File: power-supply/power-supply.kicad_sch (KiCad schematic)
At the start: 20 parts, among them J1 Barrel_Jack_Switch, J2 Output, U1 LM7812_TO220, U2 LM7912_TO220

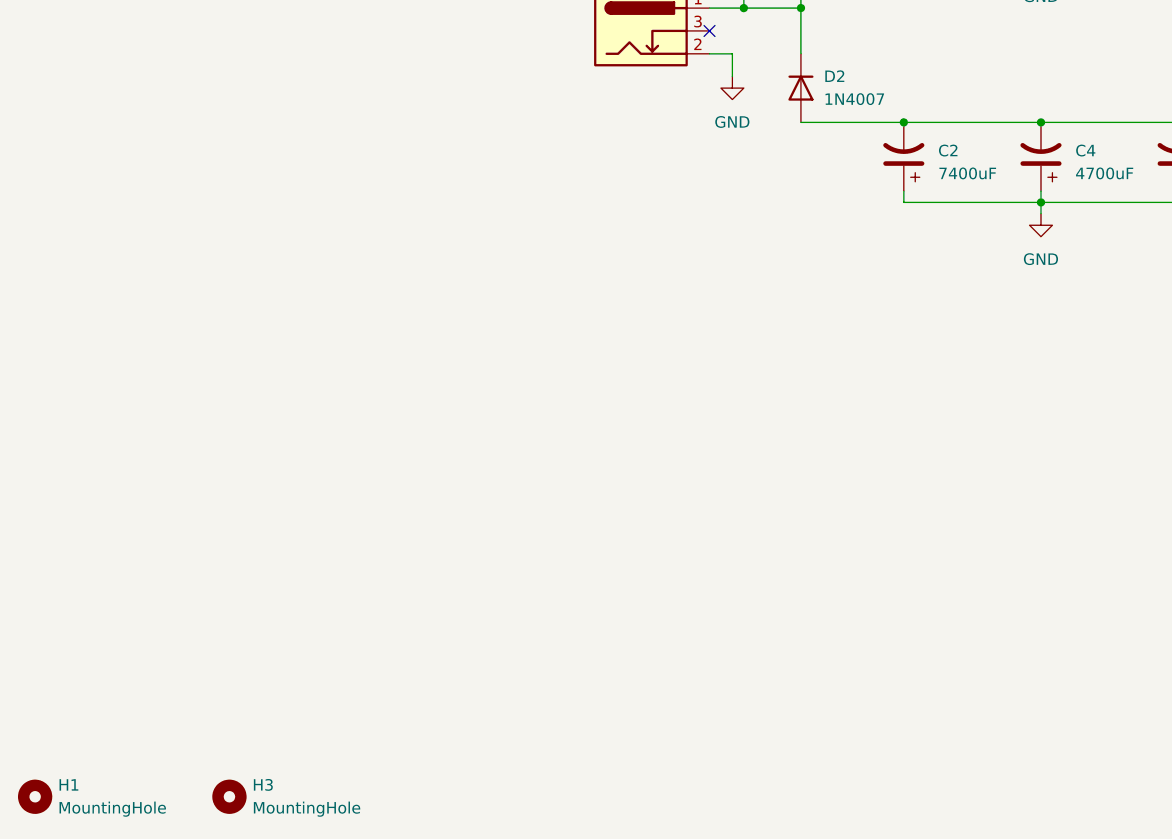
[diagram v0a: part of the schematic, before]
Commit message: Made mounting holes M3 sized. Generated BOM
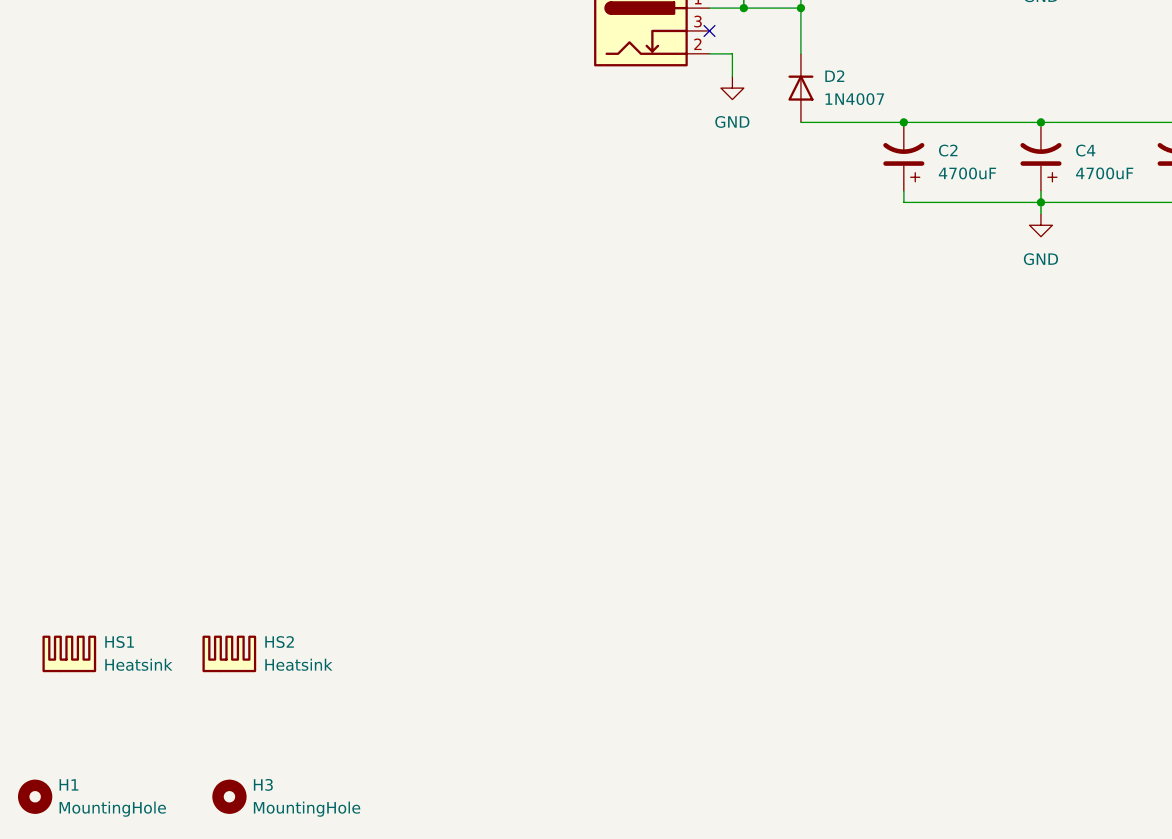
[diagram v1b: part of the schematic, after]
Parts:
- added HS1, HS2: Heatsink, symbol Mechanical:Heatsink
- C1, C3, C4, C5, C6: Manufacturer (none) -> JB Capacitors; Manufacturer Part No. (none) -> JRB1E472M07501600250000B; Supplier (none) -> Tayda; Supplier Part No. (none) -> A-1077
- C10, C7, C8, C9: Manufacturer (none) -> AVX; Manufacturer Part No. (none) -> 1uF 35V Radial Capacitor Tantalum; Supplier (none) -> Tayda; Supplier Part No. (none) -> A-265
- C2: value 7400uF -> 4700uF; Manufacturer (none) -> JB Capacitors; Manufacturer Part No. (none) -> JRB1E472M07501600250000B; Supplier (none) -> Tayda; Supplier Part No. (none) -> A-1077
- D1, D2: Manufacturer (none) -> EIC; Manufacturer Part No. (none) -> 1N4007; Supplier (none) -> Tayda; Supplier Part No. (none) -> A-155
- H1, H2, H3, H4: footprint MountingHole:MountingHole_2.2mm_M2 -> MountingHole:MountingHole_3.2mm_M3; now left out of the parts list
- J1: Manufacturer (none) -> WEALTH METAL; Manufacturer Part No. (none) -> DC Power Jack 2.1mm; Supplier (none) -> Tayda; Supplier Part No. (none) -> A-4118
- J2: Manufacturer (none) -> DEGSON; Manufacturer Part No. (none) -> DG126-03P; Supplier (none) -> Tayda; Supplier Part No. (none) -> A-663
- U1: Manufacturer (none) -> STMicroelectronics; Manufacturer Part No. (none) -> L7812CV; Supplier (none) -> Tayda; Supplier Part No. (none) -> A-207
- U2: Manufacturer (none) -> STMicroelectronics; Manufacturer Part No. (none) -> L7912CV; Supplier (none) -> Tayda; Supplier Part No. (none) -> A-505

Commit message: Updated for rev2
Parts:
- added D3: 1N4007, Diode_THT:D_DO-41_SOD81_P10.16mm_Horizontal, symbol Diode:1N4007
- C7: value 1uF -> 0.33uF
- C8: value 1uF -> 2.2uF
- C9: value 1uF -> 0.1uF
- J2: footprint TerminalBlock:TerminalBlock_Altech_AK300-3_P5.00mm -> DEGSON_Screw_Terminals:DG126
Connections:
- net at C1.1, C3.1, C5.1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: now also D3.1 (K)
- net at C9.1, J2.3 (Pin_3), U1.3 (VO): now also D3.2 (A)
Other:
- moved on the sheet: J2

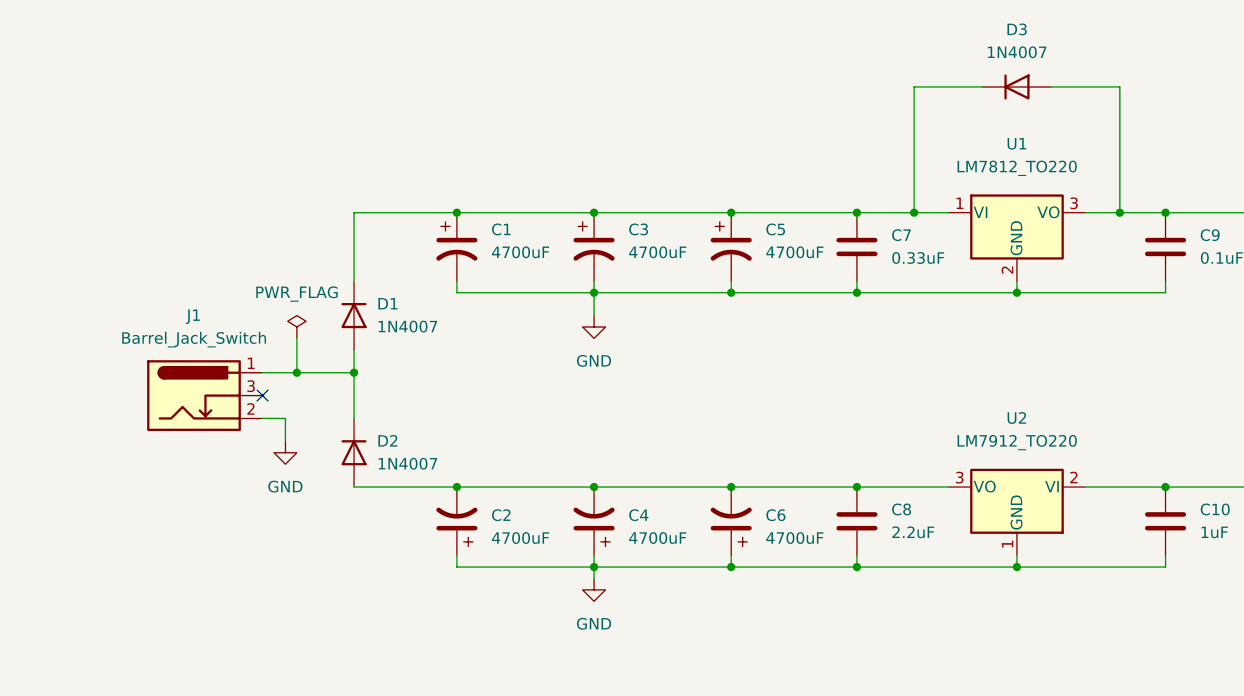
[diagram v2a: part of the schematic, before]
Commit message: Flipped input/output of 7912
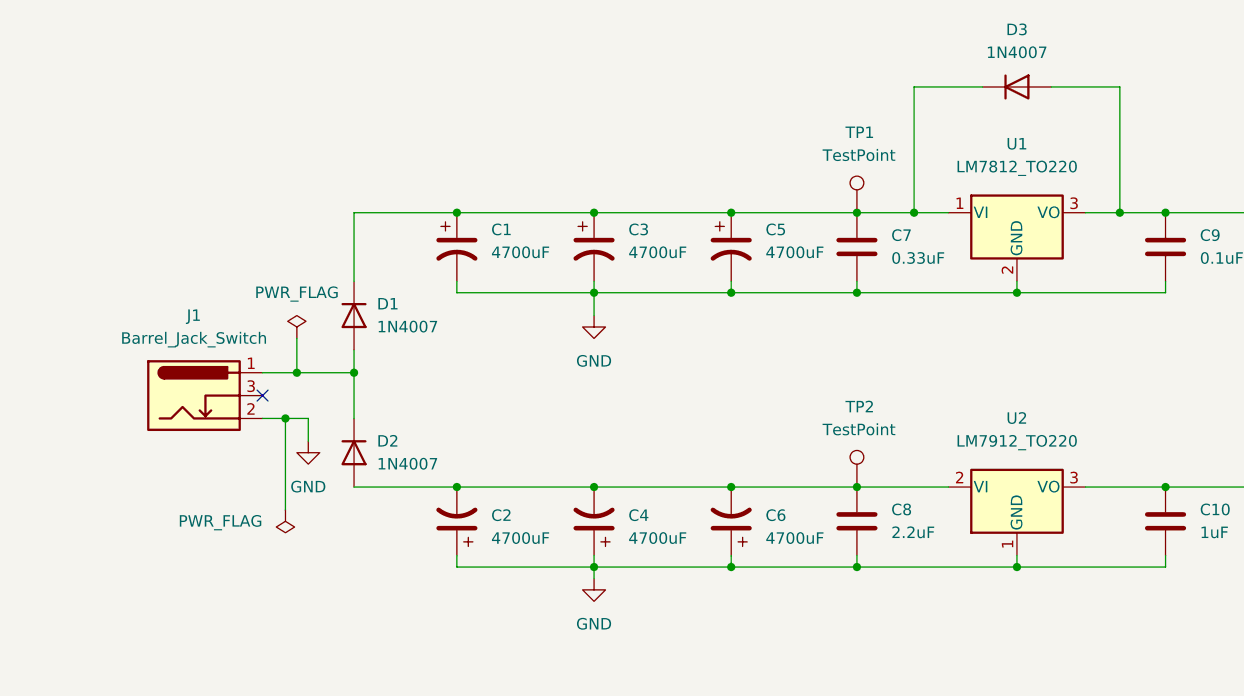
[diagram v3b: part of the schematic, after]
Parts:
- added TP1, TP2: TestPoint, TestPoint:TestPoint_Pad_D1.5mm, symbol Connector:TestPoint
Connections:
- net at C1.1, C3.1, C5.1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: now also TP1.1
- net at C2.2, C4.2, C6.2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: now also U2.2 (VI), TP2.1; no longer U2.3 (VO)
- net at C10.1, J2.1 (Pin_1): now also U2.3 (VO); no longer U2.2 (VI)
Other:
- moved on the sheet: U2
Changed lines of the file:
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@@
   (junction (at 196.85 76.2) (diameter 0) (color 0 0 0 0)
+  )
+  (junction (at 99.06 99.06) (diameter 0) (color 0 0 0 0)
   )
   (junction (at 148.59 115.57) (diameter 0) (color 0 0 0 0)
@@
     (stroke (width 0) (type default) (color 0 0 0 0))
   )
+  (wire (pts (xy 99.06 99.06) (xy 99.06 109.22))
+    (stroke (width 0) (type default) (color 0 0 0 0))
+  )
   (wire (pts (xy 133.35 115.57) (xy 148.59 115.57))
     (stroke (width 0) (type default) (color 0 0 0 0))
@@
     (stroke (width 0) (type default) (color 0 0 0 0))
   )
-  (wire (pts (xy 99.06 99.06) (xy 99.06 101.6))
+  (wire (pts (xy 101.6 99.06) (xy 101.6 101.6))
+    (stroke (width 0) (type default) (color 0 0 0 0))
+  )
+  (wire (pts (xy 99.06 99.06) (xy 101.6 99.06))
     (stroke (width 0) (type default) (color 0 0 0 0))
   )
@@
   (symbol (lib_id "power:PWR_FLAG") (at 100.33 90.17 0) (unit 1)
     (in_bom yes) (on_board yes) (fields_autoplaced)
-    (property "Reference" "#FLG01" (id 0) (at 100.33 88.265 0)
+    (property "Reference" "#FLG02" (id 0) (at 100.33 88.265 0)
       (effects (font (size 1.27 1.27)) hide)
     )
@@
     (pin "2")
   )
+  (symbol (lib_id "Connector:TestPoint") (at 162.56 76.2 0) (unit 1)
+    (in_bom yes) (on_board yes)
+    (property "Reference" "TP1" (id 0) (at 161.29 67.31 0)
+      (effects (font (size 1.27 1.27)) (justify left))
+    )
+    (property "Value" "TestPoint" (id 1) (at 158.75 69.85 0)
+      (effects (font (size 1.27 1.27)) (justify left))
+    )
+    (property "Footprint" "TestPoint:TestPoint_Pad_D1.5mm" (id 2) (at 167.64 76.2 0)
+      (effects (font (size 1.27 1.27)) hide)
+    )
+    (property "Datasheet" "~" (id 3) (at 167.64 76.2 0)
+      (effects (font (size 1.27 1.27)) hide)
+    )
+    (pin "1")
+  )
   (symbol (lib_id "Mechanical:MountingHole") (at 21.59 181.61 0) (unit 1)
     (in_bom no) (on_board yes) (fields_autoplaced)
@@
     (pin "2")
   )
-  (symbol (lib_id "Regulator_Linear:LM7912_TO220") (at 180.34 106.68 180) (unit 1)
+  (symbol (lib_id "Regulator_Linear:LM7912_TO220") (at 180.34 106.68 0) (mirror x) (unit 1)
     (in_bom yes) (on_board yes) (fields_autoplaced)
     (property "Reference" "U2" (id 0) (at 180.34 99.06 0))
@@
     (pin "2")
   )
+  (symbol (lib_id "power:PWR_FLAG") (at 99.06 109.22 0) (mirror x) (unit 1)
+    (in_bom yes) (on_board yes) (fields_autoplaced)
+    (property "Reference" "#FLG01" (id 0) (at 99.06 111.125 0)
+      (effects (font (size 1.27 1.27)) hide)
+    )
+    (property "Value" "PWR_FLAG" (id 1) (at 96.52 110.4899 0)
+      (effects (font (size 1.27 1.27)) (justify right))
+    )
+    (property "Footprint" "" (id 2) (at 99.06 109.22 0)
+      (effects (font (size 1.27 1.27)) hide)
+    )
+    (property "Datasheet" "~" (id 3) (at 99.06 109.22 0)
+      (effects (font (size 1.27 1.27)) hide)
+    )
+    (pin "1")
+  )
   (symbol (lib_id "Device:C_Polarized_US") (at 118.11 110.49 180) (unit 1)
     (in_bom yes) (on_board yes) (fields_autoplaced)
@@
     (pin "2")
   )
-  (symbol (lib_id "power:GND") (at 99.06 101.6 0) (unit 1)
-    (in_bom yes) (on_board yes) (fields_autoplaced)
-    (property "Reference" "#PWR01" (id 0) (at 99.06 107.95 0)
-      (effects (font (size 1.27 1.27)) hide)
-    )
-    (property "Value" "GND" (id 1) (at 99.06 106.68 0))
-    (property "Footprint" "" (id 2) (at 99.06 101.6 0)
-      (effects (font (size 1.27 1.27)) hide)
-    )
-    (property "Datasheet" "" (id 3) (at 99.06 101.6 0)
+  (symbol (lib_id "power:GND") (at 101.6 101.6 0) (unit 1)
+    (in_bom yes) (on_board yes)
+    (property "Reference" "#PWR01" (id 0) (at 101.6 107.95 0)
+      (effects (font (size 1.27 1.27)) hide)
+    )
+    (property "Value" "GND" (id 1) (at 101.6 106.68 0))
+    (property "Footprint" "" (id 2) (at 101.6 101.6 0)
+      (effects (font (size 1.27 1.27)) hide)
+    )
+    (property "Datasheet" "" (id 3) (at 101.6 101.6 0)
       (effects (font (size 1.27 1.27)) hide)
     )
@@
     (pin "1")
   )
+  (symbol (lib_id "Connector:TestPoint") (at 162.56 106.68 0) (unit 1)
+    (in_bom yes) (on_board yes)
+    (property "Reference" "TP2" (id 0) (at 161.29 97.79 0)
+      (effects (font (size 1.27 1.27)) (justify left))
+    )
+    (property "Value" "TestPoint" (id 1) (at 158.75 100.33 0)
+      (effects (font (size 1.27 1.27)) (justify left))
+    )
+    (property "Footprint" "TestPoint:TestPoint_Pad_D1.5mm" (id 2) (at 167.64 106.68 0)
+      (effects (font (size 1.27 1.27)) hide)
+    )
+    (property "Datasheet" "~" (id 3) (at 167.64 106.68 0)
+      (effects (font (size 1.27 1.27)) hide)
+    )
+    (pin "1")
+  )
   (symbol (lib_id "Mechanical:Heatsink") (at 25.4 167.64 0) (unit 1)
     (in_bom yes) (on_board no) (fields_autoplaced)
@@
   )
   (symbol_instances
+    (path "/54661806-454b-469b-ac8b-119e8f6e8933"
+      (reference "#FLG01") (unit 1) (value "PWR_FLAG") (footprint "")
+    )
     (path "/0a38a4d1-4822-46d9-9675-59446fc5bc25"
-      (reference "#FLG01") (unit 1) (value "PWR_FLAG") (footprint "")
+      (reference "#FLG02") (unit 1) (value "PWR_FLAG") (footprint "")
     )
     (path "/8bc0c4c3-f930-4b80-a711-d64a5e3d5cd4"
@@
       (reference "J2") (unit 1) (value "Output") (footprint "DEGSON_Screw_Terminals:DG126")
     )
+    (path "/25d93dd6-49de-420c-818e-797f7dc4cf2a"
+      (reference "TP1") (unit 1) (value "TestPoint") (footprint "TestPoint:TestPoint_Pad_D1.5mm")
+    )
+    (path "/dcf8610a-1ffe-4fa6-82d4-d960514f325a"
+      (reference "TP2") (unit 1) (value "TestPoint") (footprint "TestPoint:TestPoint_Pad_D1.5mm")
+    )
     (path "/8edc48e1-08a2-4ab3-a762-de13c48f8c3f"
